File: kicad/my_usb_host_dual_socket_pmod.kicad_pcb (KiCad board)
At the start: 2 copper layers, 38.6 x 17.4 mm, 16 parts, among them J1 USB_A_Stacked, J2 Conn_02x06_Odd_Even, J3 Conn_01x02_Socket, U2 QX2303L50T

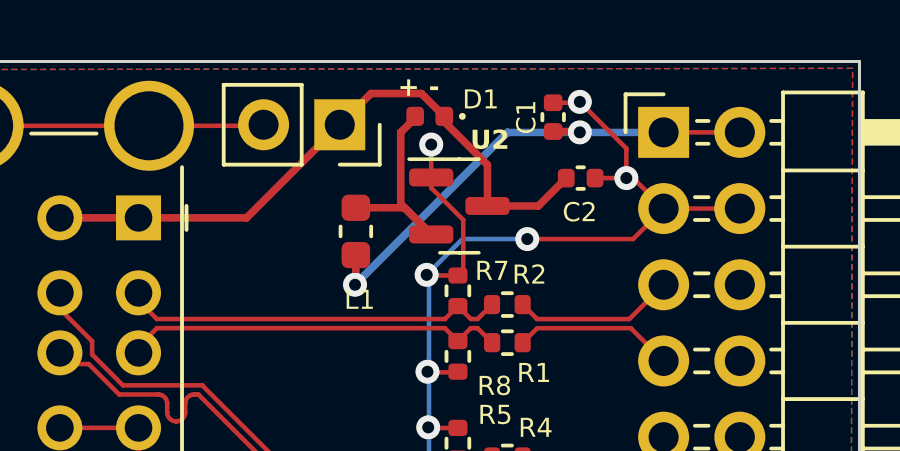
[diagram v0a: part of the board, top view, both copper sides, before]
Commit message: Replacement kicad_pcb supplied by Tavy
Replaces D1 (0402 sized) with C907849 part (DSN-2 sized)
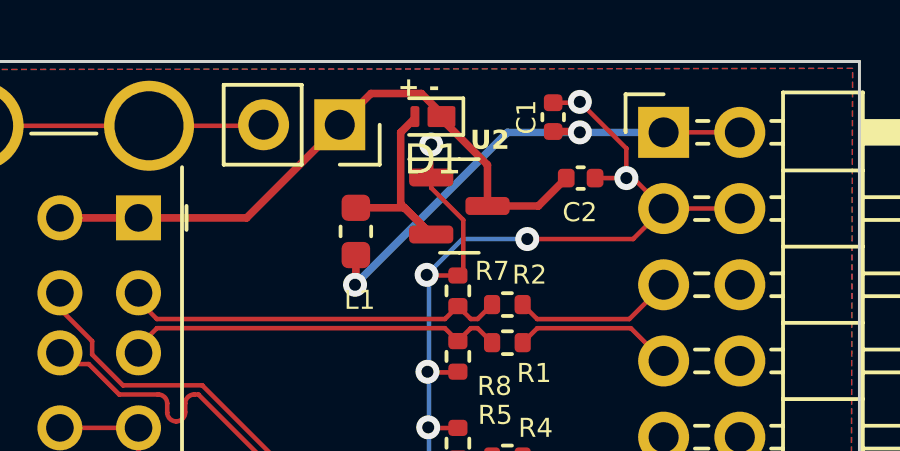
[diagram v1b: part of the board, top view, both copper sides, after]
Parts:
- D1: footprint Diode_SMD:D_0402_1005Metric -> Diode_SMD:Nexperia_DSN1608-2_1.6x0.8mm
- moved D1 0.11 mm to (96.5, 42.4)
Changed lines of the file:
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@@
     )
   )
-  (footprint "Diode_SMD:D_0402_1005Metric" (layer "F.Cu")
-    (at 96.3422 42.3926 180)
-    (descr "Diode SMD 0402 (1005 Metric), square (rectangular) end terminal, IPC_7351 nominal, (Body size source: http://www.tortai-tech.com/upload/download/2011102023233369053.pdf), generated with kicad-footprint-generator")
-    (tags "diode")
+  (footprint "Diode_SMD:Nexperia_DSN1608-2_1.6x0.8mm" (layer "F.Cu")
+    (at 96.45 42.4 180)
+    (descr "Diode SMD DSN1608, 1.6 x 0.8 x 0.29 mm, https://assets.nexperia.com/documents/package-information/SOD964.pdf")
+    (tags "diode SOD964 SOD-964")
     (property "Sheetfile" "my_usb_host_dual_socket_pmod.kicad_sch")
     (property "Sheetname" "")
@@
     (property "ki_keywords" "diode Schottky")
     (attr smd)
-    (fp_text reference "D1" (at -1.7018 0.5588 unlocked) (layer "F.SilkS")
-        (effects (font (size 0.635 0.635) (thickness 0.127)))
-    )
-    (fp_text value "1N5817/1N5819/1N5822" (at 0 1.17 unlocked) (layer "F.Fab") hide
+    (fp_text reference "D1" (at 0 -1.43 180) (layer "F.SilkS")
         (effects (font (size 1 1) (thickness 0.15)))
     )
-    (fp_text user "${REFERENCE}" (at 0 0 unlocked) (layer "F.Fab") hide
+    (fp_text value "1N5817/1N5819/1N5822" (at 0 1.43 180) (layer "F.Fab")
         (effects (font (size 1 1) (thickness 0.15)))
     )
-    (fp_circle (center -1.09 0) (end -1.04 0)
-      (stroke (width 0.127) (type solid)) (fill none) (layer "F.SilkS"))
-    (fp_line (start -0.93 -0.47) (end 0.93 -0.47)
+    (fp_text user "${REFERENCE}" (at 0 0 180) (layer "F.Fab")
+        (effects (font (size 0.4 0.4) (thickness 0.06)))
+    )
+    (fp_line (start -1.015 -0.61) (end -1.015 0.61)
+      (stroke (width 0.12) (type solid)) (layer "F.SilkS"))
+    (fp_line (start -1.015 0.61) (end 0.8 0.61)
+      (stroke (width 0.12) (type solid)) (layer "F.SilkS"))
+    (fp_line (start 0.8 -0.61) (end -1.015 -0.61)
+      (stroke (width 0.12) (type solid)) (layer "F.SilkS"))
+    (fp_line (start -1.05 -0.65) (end 1.05 -0.65)
       (stroke (width 0.05) (type solid)) (layer "F.CrtYd"))
-    (fp_line (start -0.93 0.47) (end -0.93 -0.47)
+    (fp_line (start -1.05 0.65) (end -1.05 -0.65)
       (stroke (width 0.05) (type solid)) (layer "F.CrtYd"))
-    (fp_line (start 0.93 -0.47) (end 0.93 0.47)
+    (fp_line (start 1.05 0.65) (end -1.05 0.65)
       (stroke (width 0.05) (type solid)) (layer "F.CrtYd"))
-    (fp_line (start 0.93 0.47) (end -0.93 0.47)
+    (fp_line (start 1.05 0.65) (end 1.05 -0.65)
       (stroke (width 0.05) (type solid)) (layer "F.CrtYd"))
-    (fp_line (start -0.5 -0.25) (end 0.5 -0.25)
+    (fp_line (start -0.8 -0.2) (end -0.8 0.4)
       (stroke (width 0.1) (type solid)) (layer "F.Fab"))
-    (fp_line (start -0.5 0.25) (end -0.5 -0.25)
+    (fp_line (start -0.8 0.4) (end 0.8 0.4)
       (stroke (width 0.1) (type solid)) (layer "F.Fab"))
-    (fp_line (start -0.4 0.25) (end -0.4 -0.25)
+    (fp_line (start -0.6 -0.4) (end -0.8 -0.2)
       (stroke (width 0.1) (type solid)) (layer "F.Fab"))
-    (fp_line (start -0.3 0.25) (end -0.3 -0.25)
+    (fp_line (start 0.8 -0.4) (end -0.6 -0.4)
       (stroke (width 0.1) (type solid)) (layer "F.Fab"))
-    (fp_line (start 0.5 -0.25) (end 0.5 0.25)
+    (fp_line (start 0.8 0.4) (end 0.8 -0.4)
       (stroke (width 0.1) (type solid)) (layer "F.Fab"))
-    (fp_line (start 0.5 0.25) (end -0.5 0.25)
-      (stroke (width 0.1) (type solid)) (layer "F.Fab"))
-    (pad "1" smd roundrect (at -0.485 0 180) (size 0.59 0.64) (layers "F.Cu" "F.Paste" "F.Mask") (roundrect_rratio 0.25)
+    (pad "1" smd roundrect (at -0.285 0 180) (size 0.93 0.7) (layers "F.Cu" "F.Paste" "F.Mask") (roundrect_rratio 0.1071428571)
       (net 15 "/PWR5V0") (pinfunction "K") (pintype "passive"))
-    (pad "2" smd roundrect (at 0.485 0 180) (size 0.59 0.64) (layers "F.Cu" "F.Paste" "F.Mask") (roundrect_rratio 0.25)
+    (pad "2" smd roundrect (at 0.6 0 180) (size 0.3 0.7) (layers "F.Cu" "F.Paste" "F.Mask") (roundrect_rratio 0.25)
       (net 5 "Net-(D1-A)") (pinfunction "A") (pintype "passive"))
-    (model "${KICAD6_3DMODEL_DIR}/Diode_SMD.3dshapes/D_0402_1005Metric.wrl"
+    (model "${KICAD7_3DMODEL_DIR}/Diode_SMD.3dshapes/Nexperia_DSN1608-2_1.6x0.8mm.wrl"
       (offset (xyz 0 0 0))
       (scale (xyz 1 1 1))
